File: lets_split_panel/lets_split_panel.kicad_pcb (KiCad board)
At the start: 2 copper layers, 230.5 x 82 mm, 164 parts, among them J1 Speaker, J2 RST, J3 ISP, J4 RST, J5 Speaker, J6 ISP, P1 WS2812>, P2 USB_OTG, P3 >WS2812, P4 Conn_01x04, P5 USB_OTG, P6 >WS2812, P7 WS2812>, P8 Conn_01x04, SW1 MXALPS, SW10 MXALPS, SW11 MXALPS, SW12 MXALPS, SW13 MXALPS, SW14 MXALPS, SW15 MXALPS, SW16 MXALPS, SW17 MXALPS, SW18 MXALPS, SW19 MXALPS, SW2 MXALPS, SW20 MXALPS, SW21 MXALPS, SW22 MXALPS, SW23 MXALPS, SW24 MXALPS, SW25 MXALPS, SW26 MXALPS, SW27 MXALPS, SW28 MXALPS, SW29 MXALPS, SW3 MXALPS, SW30 MXALPS, SW31 MXALPS, SW32 MXALPS, SW33 MXALPS, SW34 MXALPS, SW35 MXALPS, SW36 MXALPS, SW37 MXALPS, SW38 MXALPS, SW39 MXALPS, SW4 MXALPS, SW40 MXALPS, SW41 MXALPS, SW42 MXALPS, SW43 MXALPS, SW44 MXALPS, SW45 MXALPS, SW46 MXALPS, SW47 MXALPS, SW48 MXALPS, SW5 MXALPS, SW6 MXALPS, SW7 MXALPS, SW8 MXALPS, SW9 MXALPS, U1 ATMega32U4, U2 ATMega32U4, Y1 Crystal, Y2 Crystal

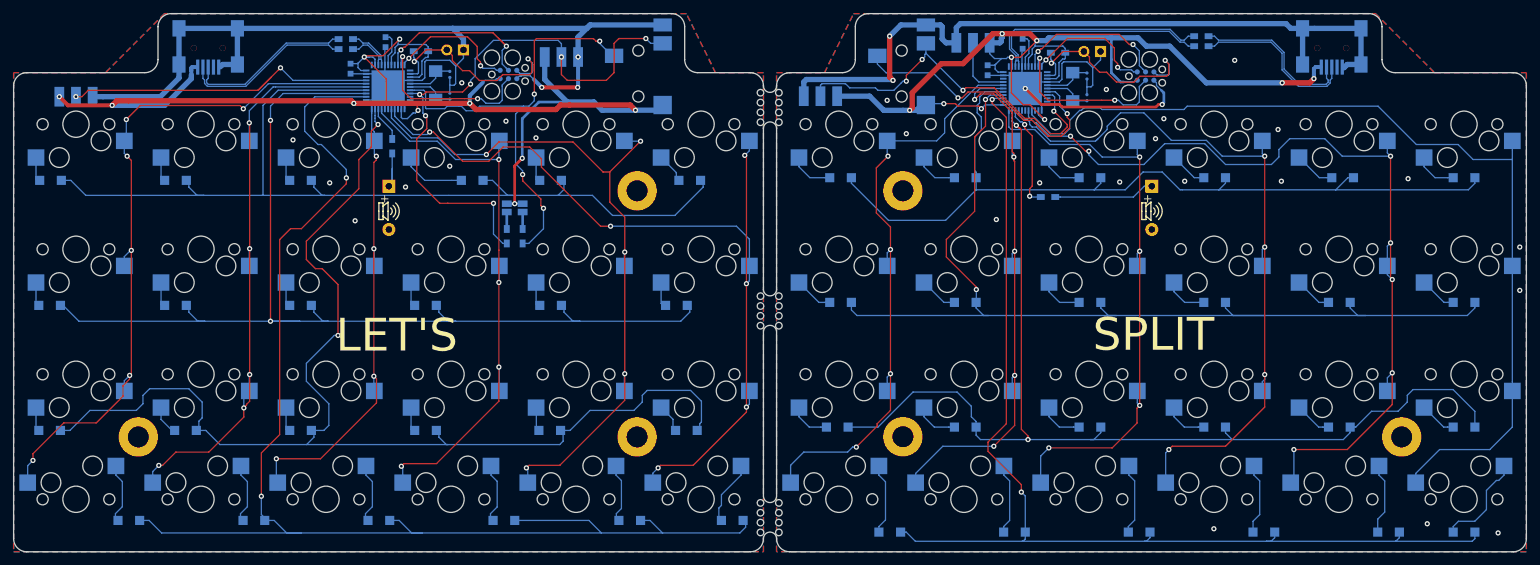
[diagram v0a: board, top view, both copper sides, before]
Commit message: Added test jig for panel
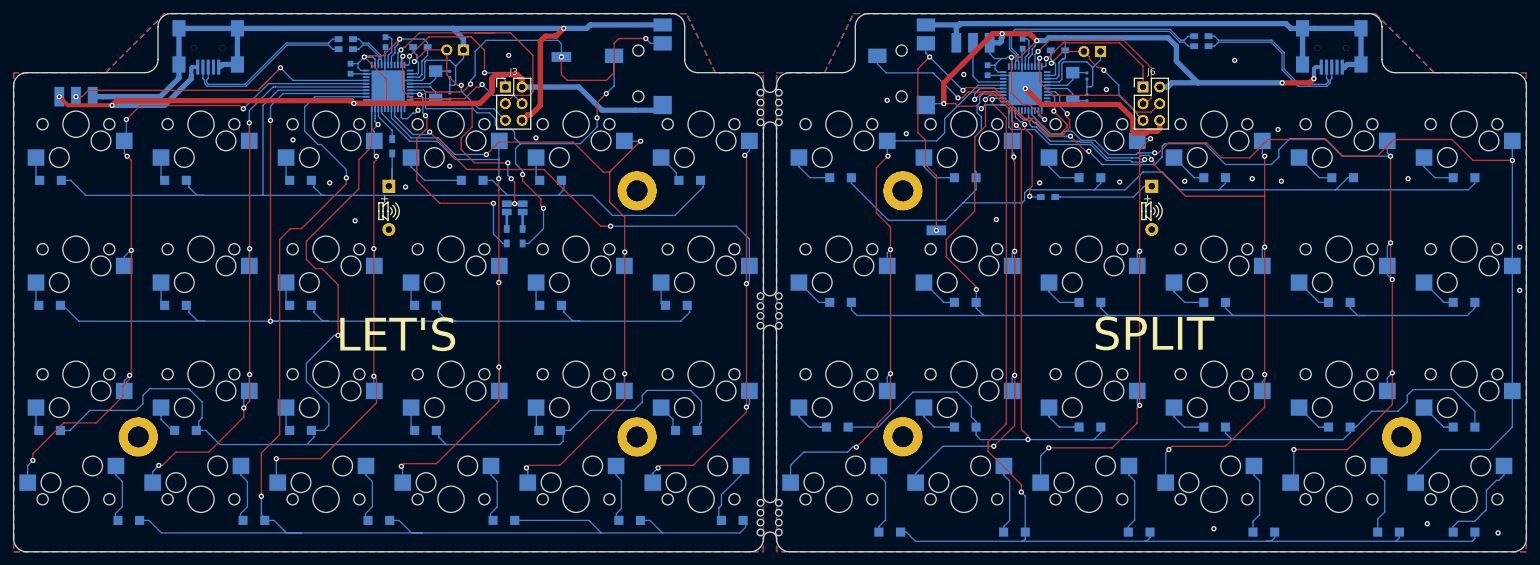
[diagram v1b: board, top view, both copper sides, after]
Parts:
- removed P1, P7: WS2812>, Wirepads:SMD_PAD_1x03_Pitch2.54mm
- added J7: WS2812>, Pin_Headers:Pin_Header_Straight_1x01_Pitch2.54mm, B.Cu at (107.5, 62.6)
- added J8: WS2812>, Pin_Headers:Pin_Header_Straight_1x01_Pitch2.54mm, B.Cu at (164.6, 89.0)
- J3, J6: footprint Jlink:J-link-needle-6pin -> Pin_Headers:Pin_Header_Straight_2x03_Pitch2.54mm; moved to F.Cu
- moved J3 2.82 mm to (98.9, 67.2)
- moved J6 2.72 mm to (196.1, 67.2)
- moved R6 0.64 mm to (86.0, 61.1)
- moved R9 0.37 mm to (183.1, 61.6)
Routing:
- net VBUS: track 387.8 -> 335.3 mm, vias 19 -> 17
- net GND: track 358.2 -> 323.9 mm, vias 33 -> 27
- net /Left half/SCK: track 26.5 -> 38.3 mm, vias 2 -> 1
- net /Right half/~RESET: track 34.1 -> 25.9 mm
- net /Right half/SDA: track 56.9 -> 63.9 mm
- net /Left half/~Reset: track 34.1 -> 28.2 mm
- net /Right half/col2: track 93.2 -> 98.6 mm, vias 4 -> 5
- net /Left half/SCL/D3: track 71.3 -> 66.5 mm
- net /Right half/SCK: track 23.6 -> 28.4 mm, vias 2 -> 1
- net /Right half/col5: track 143.8 -> 147.7 mm, vias 0 -> 2
- net /Left half/MISO: track 20.1 -> 23.7 mm
- net /Right half/row0: track 130.6 -> 134.1 mm
- net /Left half/col5: track 136.7 -> 134.1 mm
- net /Right half/MISO: track 20.1 -> 22.2 mm, vias 2 -> 1
- net /Left half/MOSI: track 26.4 -> 27.5 mm
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
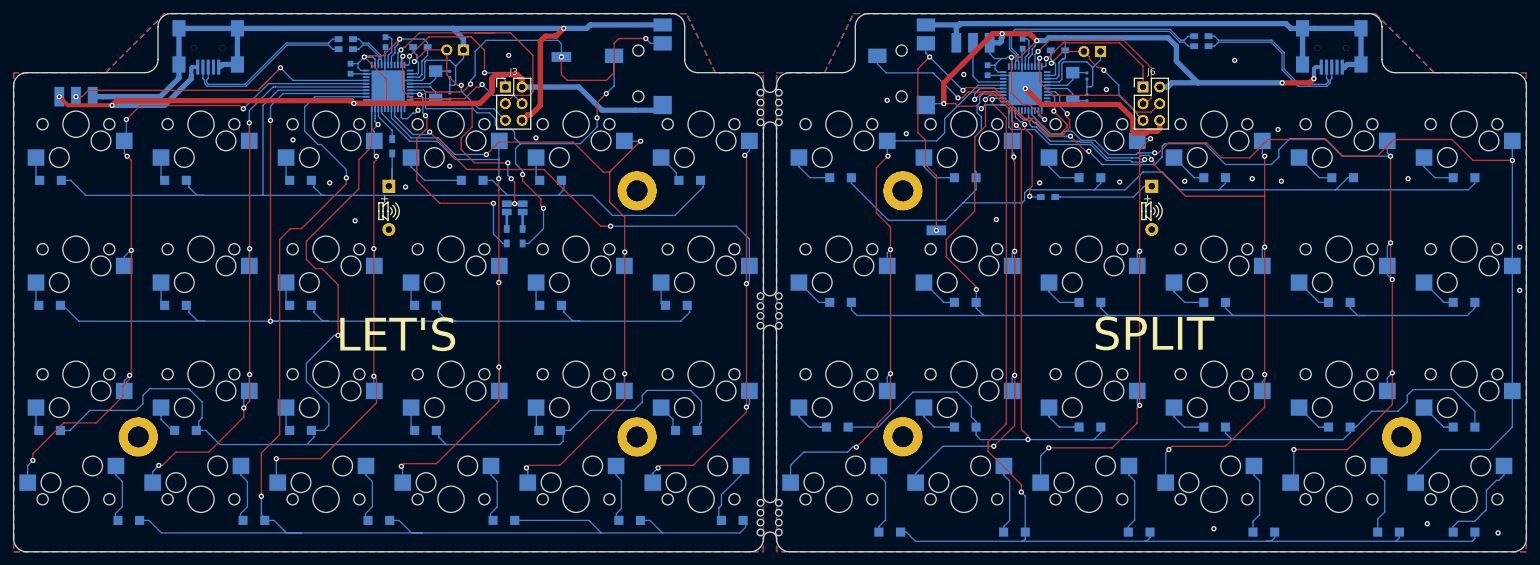
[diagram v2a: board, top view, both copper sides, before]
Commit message: Added 3D models
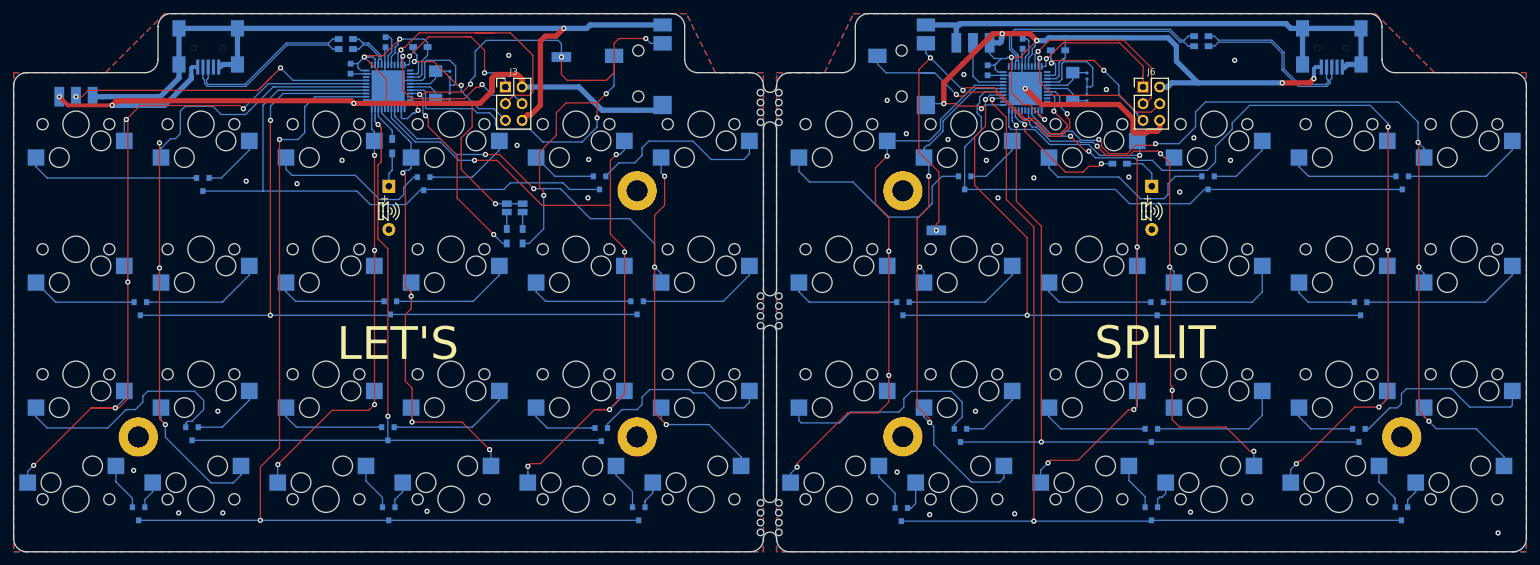
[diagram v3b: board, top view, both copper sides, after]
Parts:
- removed D25, D26, D27, D28, D29, D30, D31, D32, D33, D34, D35, D36, D37, D38, D39, D40, D41, D42, D43, D44, D45, D46, D47, D48: D, SeeedOPL-Diode-2016:SOD-123
- removed J2, J4: RST, Pin_Headers:Pin_Header_Straight_1x02_Pitch2.54mm
- D1, D10, D11, D12, D13, D14, D15, D16, D17, D18, D19, D2, D20, D21, D22, D23, D24, D3, D4, D5, D6, D7, D8, D9: value D -> D_x2_KCom_AAK; footprint SeeedOPL-Diode-2016:SOD-123 -> TO_SOT_Packages_SMD:SOT-23
- SW1, SW10, SW11, SW12, SW13, SW14, SW15, SW16, SW17, SW18, SW19, SW2, SW20, SW21, SW22, SW23, SW24, SW25, SW26, SW27, SW28, SW29, SW3, SW30, SW31, SW32, SW33, SW34, SW35, SW36, SW37, SW38, SW39, SW4, SW40, SW41, SW42, SW43, SW44, SW45, SW46, SW47, SW48, SW5, SW6, SW7, SW8, SW9: value MXALPS -> Socket
- moved D15 153.5 mm to (235.6, 81.8), turned to 270 degrees
- moved D18 123.4 mm to (229.2, 101.0), turned to 270 degrees
- moved D14 120.7 mm to (206.0, 81.8), turned to 270 degrees
- moved D21 109.1 mm to (229.0, 120.3), turned to 270 degrees
- moved D24 102.0 mm to (235.5, 132.2), turned to 270 degrees
- moved D17 94.5 mm to (198.2, 101.0), turned to 270 degrees
- moved D3 91.9 mm to (113.3, 81.8), turned to 270 degrees
- moved D20 80.5 mm to (197.4, 120.3), turned to 270 degrees
- moved D13 75.0 mm to (168.9, 81.8), turned to 270 degrees
- moved D23 72.0 mm to (197.4, 132.2), turned to 270 degrees
- moved D6 70.3 mm to (119.0, 100.8), turned to 270 degrees
- moved D16 68.8 mm to (159.5, 101.0), turned to 270 degrees
- moved D19 62.6 mm to (168.3, 120.3), turned to 270 degrees
- moved D9 60.0 mm to (113.5, 120.1), turned to 270 degrees
- moved D2 59.9 mm to (86.5, 81.9), turned to 270 degrees
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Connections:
- D1 pad 1: /Left half/row0 -> Net-(D1-Pad1)
- D10 pad 1: /Left half/row1 -> Net-(D10-Pad1)
- D11 pad 1: /Left half/row2 -> Net-(D11-Pad1)
- D12 pad 1: /Left half/row3 -> Net-(D12-Pad1)
- D13 pad 1: /Left half/row0 -> Net-(D13-Pad1)
- D14 pad 1: /Left half/row1 -> Net-(D14-Pad1)
- D15 pad 1: /Left half/row2 -> Net-(D15-Pad1)
- D16 pad 1: /Left half/row3 -> Net-(D16-Pad1)
- D17 pad 1: /Left half/row0 -> Net-(D17-Pad1)
- D18 pad 1: /Left half/row1 -> Net-(D18-Pad1)
- D19 pad 1: /Left half/row2 -> Net-(D19-Pad1)
- D2 pad 1: /Left half/row1 -> Net-(D2-Pad1)
- D20 pad 1: /Left half/row3 -> Net-(D20-Pad1)
- D21 pad 1: /Left half/row0 -> Net-(D21-Pad1)
- D22 pad 1: /Left half/row1 -> Net-(D22-Pad1)
- D23 pad 1: /Left half/row2 -> Net-(D23-Pad1)
- D24 pad 1: /Left half/row3 -> Net-(D24-Pad1)
- D3 pad 1: /Left half/row2 -> Net-(D3-Pad1)
- D4 pad 1: /Left half/row3 -> Net-(D4-Pad1)
- D5 pad 1: /Left half/row0 -> Net-(D5-Pad1)
- D6 pad 1: /Left half/row1 -> Net-(D6-Pad1)
- D7 pad 1: /Left half/row2 -> Net-(D7-Pad1)
- D8 pad 1: /Left half/row3 -> Net-(D8-Pad1)
- D9 pad 1: /Left half/row0 -> Net-(D9-Pad1)
- SW1 pad 2: Net-(D1-Pad2) -> Net-(D1-Pad1)
- SW10 pad 1: /Left half/col3 -> Net-(D5-Pad2)
- SW10 pad 2: Net-(D14-Pad2) -> /Left half/col3
- SW11 pad 2: Net-(D18-Pad2) -> Net-(D6-Pad1)
- SW12 pad 1: /Left half/col5 -> Net-(D6-Pad2)
- SW12 pad 2: Net-(D22-Pad2) -> /Left half/col5
- SW13 pad 2: Net-(D3-Pad2) -> Net-(D7-Pad1)
- SW14 pad 1: /Left half/col1 -> Net-(D7-Pad2)
- SW14 pad 2: Net-(D7-Pad2) -> /Left half/col1
- SW15 pad 2: Net-(D11-Pad2) -> Net-(D8-Pad1)
- SW16 pad 1: /Left half/col3 -> Net-(D8-Pad2)
- SW16 pad 2: Net-(D15-Pad2) -> /Left half/col3
- SW17 pad 2: Net-(D19-Pad2) -> Net-(D9-Pad1)
- SW18 pad 1: /Left half/col5 -> Net-(D9-Pad2)
- SW18 pad 2: Net-(D23-Pad2) -> /Left half/col5
- SW19 pad 2: Net-(D4-Pad2) -> Net-(D10-Pad1)
- SW2 pad 1: /Left half/col1 -> Net-(D1-Pad2)
- SW2 pad 2: Net-(D5-Pad2) -> /Left half/col1
- SW20 pad 1: /Left half/col1 -> Net-(D10-Pad2)
- SW20 pad 2: Net-(D8-Pad2) -> /Left half/col1
- SW21 pad 2: Net-(D12-Pad2) -> Net-(D11-Pad1)
- SW22 pad 1: /Left half/col3 -> Net-(D11-Pad2)
- SW22 pad 2: Net-(D16-Pad2) -> /Left half/col3
- SW23 pad 2: Net-(D20-Pad2) -> Net-(D12-Pad1)
- SW24 pad 1: /Left half/col5 -> Net-(D12-Pad2)
- SW24 pad 2: Net-(D24-Pad2) -> /Left half/col5
- SW25 pad 2: Net-(D25-Pad2) -> Net-(D13-Pad1)
- SW26 pad 1: /Right half/col1 -> Net-(D13-Pad2)
- SW26 pad 2: Net-(D29-Pad2) -> /Right half/col1
- SW27 pad 2: Net-(D33-Pad2) -> Net-(D14-Pad1)
- SW28 pad 1: /Right half/col3 -> Net-(D14-Pad2)
- SW28 pad 2: Net-(D37-Pad2) -> /Right half/col3
- SW29 pad 2: Net-(D41-Pad2) -> Net-(D15-Pad1)
- SW3 pad 2: Net-(D9-Pad2) -> Net-(D2-Pad1)
- SW30 pad 1: /Right half/col5 -> Net-(D15-Pad2)
- SW30 pad 2: Net-(D45-Pad2) -> /Right half/col5
- SW31 pad 2: Net-(D26-Pad2) -> Net-(D16-Pad1)
- SW32 pad 1: /Right half/col1 -> Net-(D16-Pad2)
- SW32 pad 2: Net-(D30-Pad2) -> /Right half/col1
- SW33 pad 2: Net-(D34-Pad2) -> Net-(D17-Pad1)
- SW34 pad 1: /Right half/col3 -> Net-(D17-Pad2)
- SW34 pad 2: Net-(D38-Pad2) -> /Right half/col3
- SW35 pad 2: Net-(D42-Pad2) -> Net-(D18-Pad1)
- SW36 pad 1: /Right half/col5 -> Net-(D18-Pad2)
- SW36 pad 2: Net-(D46-Pad2) -> /Right half/col5
- SW37 pad 2: Net-(D27-Pad2) -> Net-(D19-Pad1)
- SW38 pad 1: /Right half/col1 -> Net-(D19-Pad2)
- SW38 pad 2: Net-(D31-Pad2) -> /Right half/col1
- SW39 pad 2: Net-(D35-Pad2) -> Net-(D20-Pad1)
- SW4 pad 1: /Left half/col3 -> Net-(D2-Pad2)
- SW4 pad 2: Net-(D13-Pad2) -> /Left half/col3
- SW40 pad 1: /Right half/col3 -> Net-(D20-Pad2)
- SW40 pad 2: Net-(D39-Pad2) -> /Right half/col3
- SW41 pad 2: Net-(D43-Pad2) -> Net-(D21-Pad1)
- SW42 pad 1: /Right half/col5 -> Net-(D21-Pad2)
- SW42 pad 2: Net-(D47-Pad2) -> /Right half/col5
- SW43 pad 2: Net-(D28-Pad2) -> Net-(D22-Pad1)
- SW44 pad 1: /Right half/col1 -> Net-(D22-Pad2)
- SW44 pad 2: Net-(D32-Pad2) -> /Right half/col1
- SW45 pad 2: Net-(D36-Pad2) -> Net-(D23-Pad1)
- SW46 pad 1: /Right half/col3 -> Net-(D23-Pad2)
- SW46 pad 2: Net-(D40-Pad2) -> /Right half/col3
- SW47 pad 2: Net-(D44-Pad2) -> Net-(D24-Pad1)
- SW48 pad 1: /Right half/col5 -> Net-(D24-Pad2)
- SW48 pad 2: Net-(D48-Pad2) -> /Right half/col5
- SW5 pad 2: Net-(D17-Pad2) -> Net-(D3-Pad1)
- SW6 pad 1: /Left half/col5 -> Net-(D3-Pad2)
- SW6 pad 2: Net-(D21-Pad2) -> /Left half/col5
- SW7 pad 2: Net-(D2-Pad2) -> Net-(D4-Pad1)
- SW8 pad 1: /Left half/col1 -> Net-(D4-Pad2)
- SW8 pad 2: Net-(D6-Pad2) -> /Left half/col1
- SW9 pad 2: Net-(D10-Pad2) -> Net-(D5-Pad1)
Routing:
- net /Left half/row2: track 185.0 -> 114.1 mm
- net /Left half/row0: track 147.7 -> 92.8 mm
- net /Right half/row2: track 167.3 -> 113.1 mm
- net /Left half/row3: track 205.5 -> 154.0 mm
- net /Right half/row0: track 134.1 -> 88.0 mm
- net /Right half/row1: track 153.8 -> 109.6 mm
- net /Left half/row1: track 166.6 -> 123.0 mm
- net Net-(D7-Pad1): track 0.00 -> 36.7 mm
- net Net-(D19-Pad1): track 0.00 -> 35.0 mm
- net Net-(D13-Pad1): track 0.00 -> 33.4 mm
- net Net-(D14-Pad1): track 0.00 -> 29.2 mm
- net Net-(D1-Pad1): track 0.00 -> 26.6 mm
- net Net-(D2-Pad1): track 0.00 -> 25.8 mm
- net Net-(D21-Pad2): track 4.45 -> 29.3 mm
- net Net-(D3-Pad2): track 3.49 -> 28.3 mm
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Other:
- board text removed: "RST"

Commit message: Added option for 2U spacebars
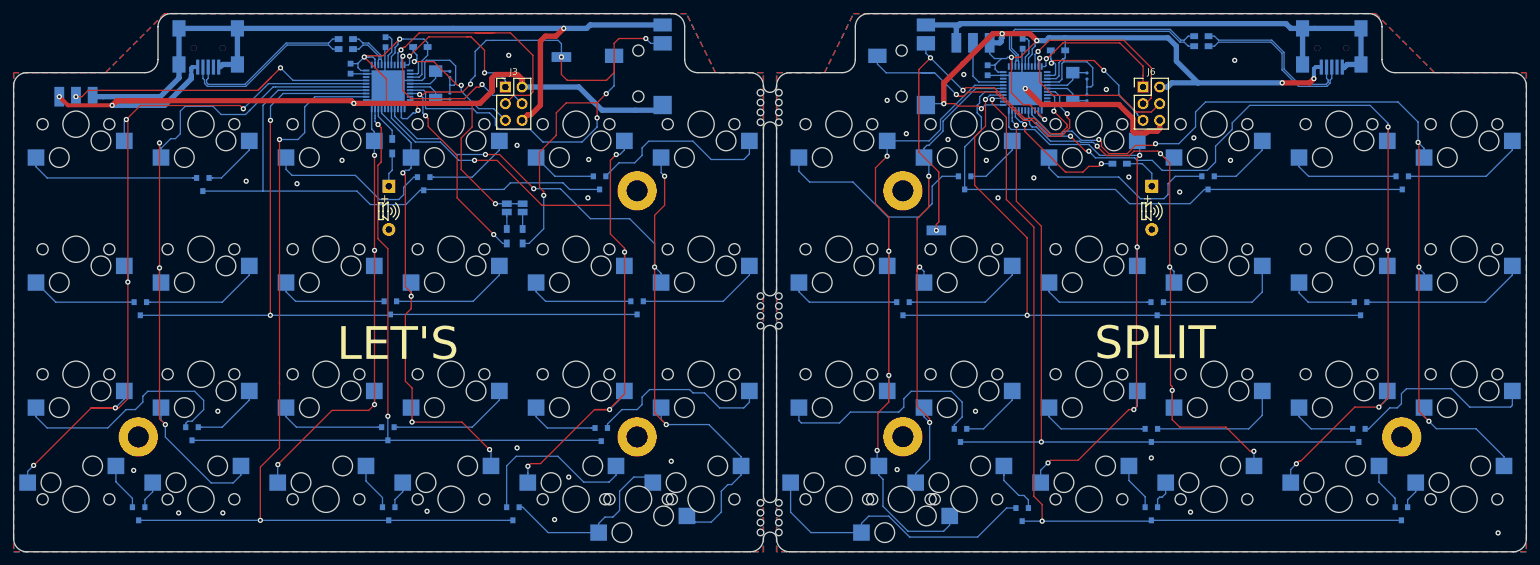
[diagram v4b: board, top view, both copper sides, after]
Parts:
- added SW24: Socket, CherryMX:Kailh-socket, F.Cu at (119.2, 130.0)
- added SW43: Socket, CherryMX:Kailh-socket, F.Cu at (149.8, 130.0)
- moved D12 19.2 mm to (100.1, 132.2)
- moved D22 18.4 mm to (177.7, 132.3)
- moved SW43 9.53 mm to (159.3, 130.0), turned to 180 degrees
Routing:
- net Net-(D22-Pad1): track 7.44 -> 45.1 mm
- net Net-(D12-Pad2): track 4.24 -> 28.4 mm
- net Net-(D12-Pad1): track 7.33 -> 27.0 mm
- net /Left half/row3: track 154.0 -> 134.8 mm
- net /Right half/row3: track 144.9 -> 127.0 mm
- net /Left half/col5: track 115.1 -> 130.0 mm
- net /Right half/col0: track 89.5 -> 98.8 mm
- net /Right half/col1: track 85.2 -> 76.5 mm
- net Net-(D22-Pad2): track 4.71 -> 8.42 mm
- net GND: vias 33 -> 36

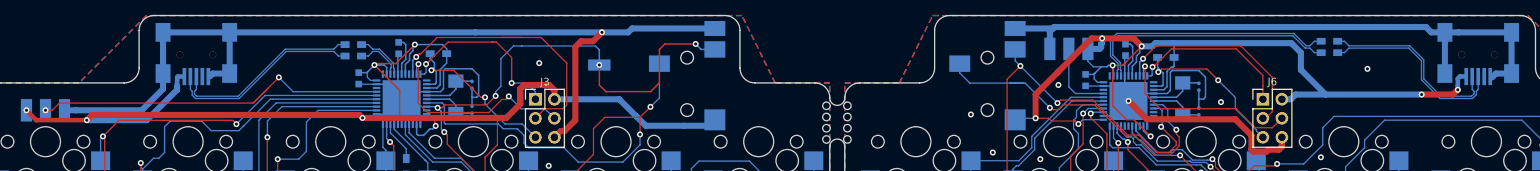
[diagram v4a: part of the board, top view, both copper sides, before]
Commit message: made sure USB datalines had gnd under them
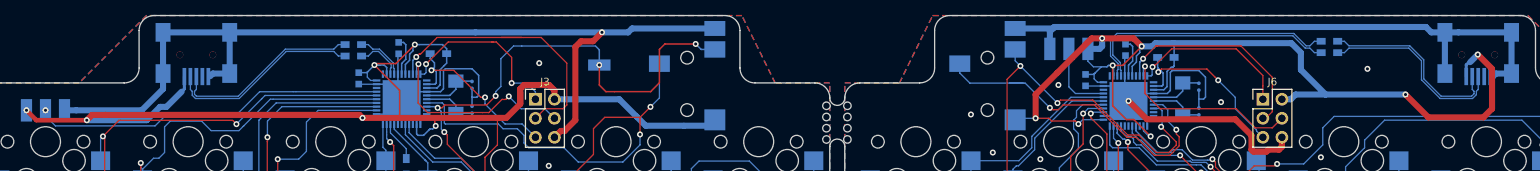
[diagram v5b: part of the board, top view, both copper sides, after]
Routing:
- net VBUS: track 332.8 -> 346.6 mm
- net /Left half/wd2812-in: track 49.7 -> 47.4 mm, vias 2 -> 1
